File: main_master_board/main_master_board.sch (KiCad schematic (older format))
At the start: 21 parts, among them P1 Hebi_1, P13 CONN_02X20, P2 Hebi_2, P3 Vbackup, P4 CONN_02X05, P5 Mounting Holes, P6 Mounting Holes, P7 Mounting Holes, P8 Mounting Holes, Q3 PSMN013-80YS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

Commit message: Changed expansion connector to two connectors. Routed 5 to 4 buck.
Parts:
- removed P13: CONN_02X20, Hirose:DF40HC(3.0)-40DS-0.4V(51), symbol CONN_02X20
- added P13, P15: CONN_02X15, Hirose:DF40HC(3.5)-30DS-0.4V(51), symbol CONN_02X15
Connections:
- net labels added: GPIO_105, GPIO_106, GPIO_108, GPIO_113, GPIO_114, GPIO_116, GPIO_26, GPIO_27, GPIO_28, GPIO_30, GPIO_49, GPIO_50, GPIO_51, GPIO_52, GPIO_69
- net labels removed: RD9, RF2
- wire segments 215 -> 256
- no-connect marks 1 -> 0
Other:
- moved on the sheet: P5, P6, P7, P8

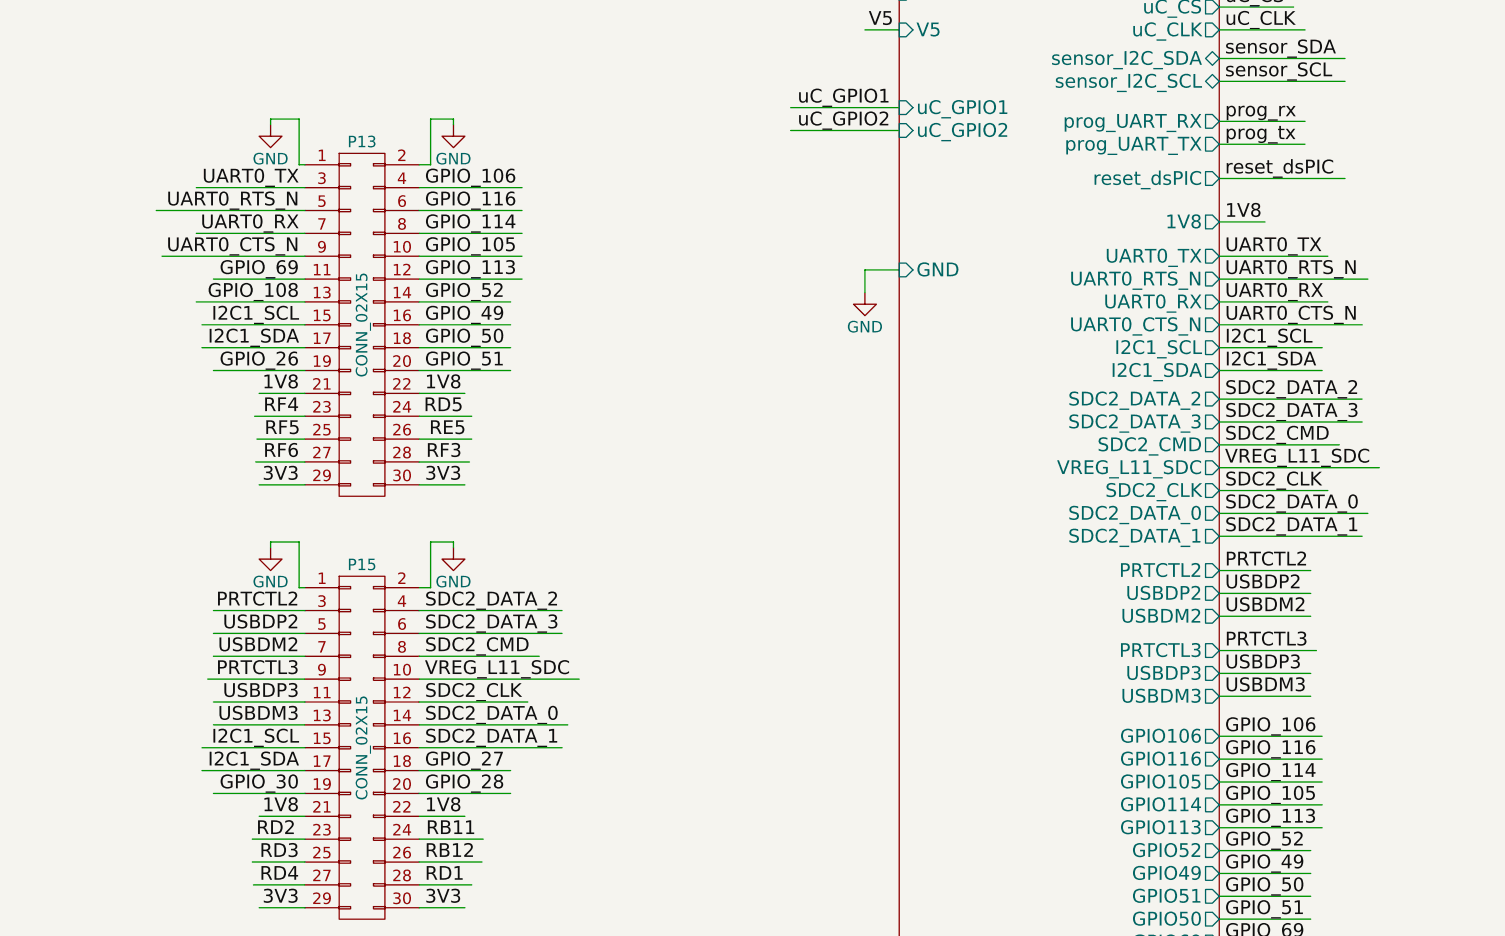
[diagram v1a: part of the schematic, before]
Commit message: Added antenna for DART board. Also fixed 90 pin connector placement (was 180 degrees wrong). Placed Dart Board in position.
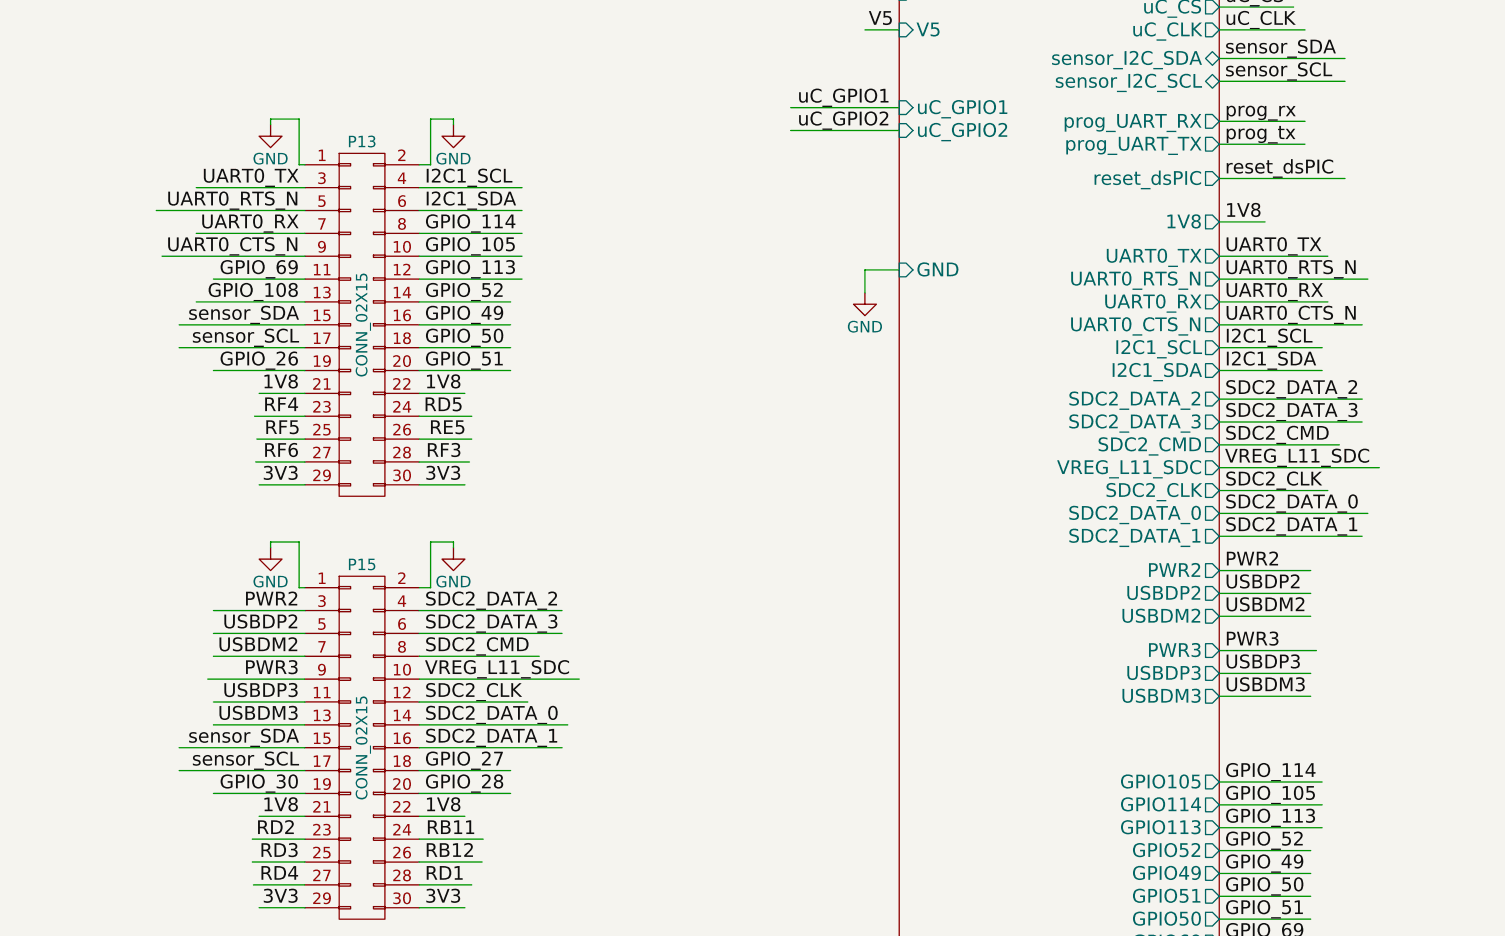
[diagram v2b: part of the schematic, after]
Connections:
- net labels added: PWR2, PWR3
- net labels removed: GPIO_106, GPIO_116, PRTCTL2, PRTCTL3
- wire segments 256 -> 254

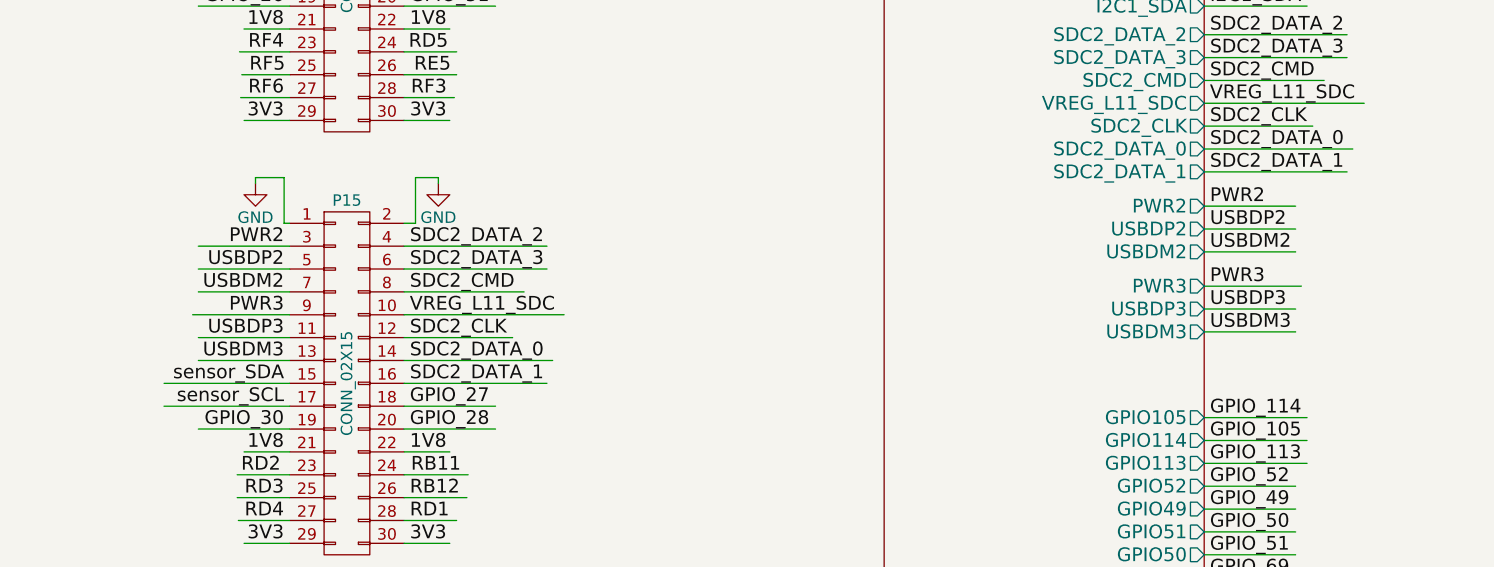
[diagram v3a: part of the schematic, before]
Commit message: Started differential routing for USB and Ethernet.
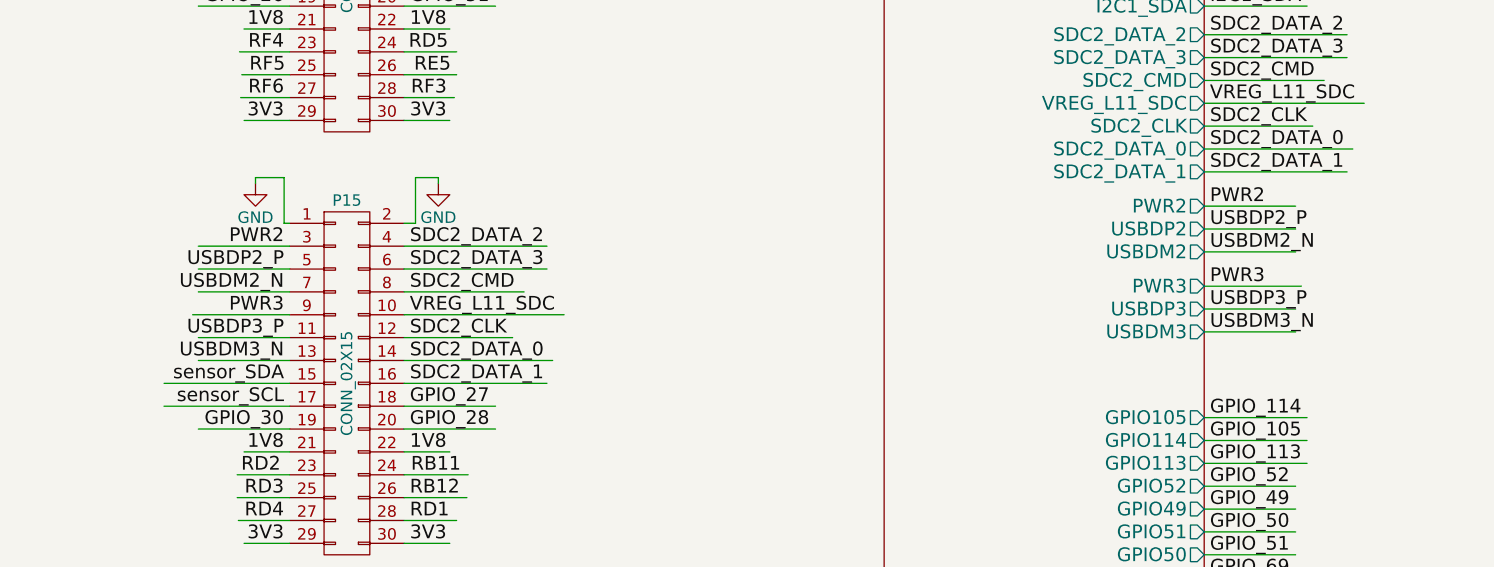
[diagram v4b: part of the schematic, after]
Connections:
- net labels added: USBDM2_N, USBDM3_N, USBDP2_P, USBDP3_P
- net labels removed: USBDM2, USBDM3, USBDP2, USBDP3
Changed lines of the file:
@@
 3V3
 $Comp
-L GNDPWR #PWR8
+L GNDPWR #PWR01
 U 1 1 58756896
 P 2760 2450
-F 0 "#PWR8" H 2760 2250 50  0001 C CNN
+F 0 "#PWR01" H 2760 2250 50  0001 C CNN
 F 1 "GNDPWR" H 2760 2320 50  0000 C CNN
 F 2 "" H 2760 2400 50  0000 C CNN
@@
 $EndComp
 $Comp
-L GND #PWR11
+L GND #PWR02
 U 1 1 58756928
 P 4330 2440
-F 0 "#PWR11" H 4330 2190 50  0001 C CNN
+F 0 "#PWR02" H 4330 2190 50  0001 C CNN
 F 1 "GND" H 4330 2290 50  0000 C CNN
 F 2 "" H 4330 2440 50  0000 C CNN
@@
 Vmotors
 $Comp
-L GND #PWR17
+L GND #PWR03
 U 1 1 5875B134
 P 5225 1790
-F 0 "#PWR17" H 5225 1540 50  0001 C CNN
+F 0 "#PWR03" H 5225 1540 50  0001 C CNN
 F 1 "GND" H 5225 1640 50  0000 C CNN
 F 2 "" H 5225 1790 50  0000 C CNN
@@
 $EndComp
 $Comp
-L GNDPWR #PWR16
+L GNDPWR #PWR04
 U 1 1 5875E5EF
 P 4975 1810
-F 0 "#PWR16" H 4975 1610 50  0001 C CNN
+F 0 "#PWR04" H 4975 1610 50  0001 C CNN
 F 1 "GNDPWR" H 4975 1680 50  0000 C CNN
 F 2 "" H 4975 1760 50  0000 C CNN
@@
 $EndSheet
 $Comp
-L GND #PWR24
+L GND #PWR05
 U 1 1 587B1461
 P 15990 965
-F 0 "#PWR24" H 15990 715 50  0001 C CNN
+F 0 "#PWR05" H 15990 715 50  0001 C CNN
 F 1 "GND" H 15990 815 50  0000 C CNN
 F 2 "" H 15990 965 50  0000 C CNN
@@
 prog_tx
 $Comp
-L GND #PWR23
+L GND #PWR06
 U 1 1 588455B7
 P 13230 6340
-F 0 "#PWR23" H 13230 6090 50  0001 C CNN
+F 0 "#PWR06" H 13230 6090 50  0001 C CNN
 F 1 "GND" H 13230 6190 50  0000 C CNN
 F 2 "" H 13230 6340 50  0000 C CNN
@@
 sensor_SCL
 $Comp
-L GND #PWR22
+L GND #PWR07
 U 1 1 5889E95F
 P 9450 4460
-F 0 "#PWR22" H 9450 4210 50  0001 C CNN
+F 0 "#PWR07" H 9450 4210 50  0001 C CNN
 F 1 "GND" H 9450 4310 50  0000 C CNN
 F 2 "" H 9450 4460 50  0000 C CNN
@@
 Vbackup_in
 $Comp
-L GND #PWR9
+L GND #PWR08
 U 1 1 588D5080
 P 2780 3385
-F 0 "#PWR9" H 2780 3135 50  0001 C CNN
+F 0 "#PWR08" H 2780 3135 50  0001 C CNN
 F 1 "GND" H 2780 3235 50  0000 C CNN
 F 2 "" H 2780 3385 50  0000 C CNN
@@
 V_hebi1
 $Comp
-L GNDPWR #PWR15
+L GNDPWR #PWR09
 U 1 1 588D5095
 P 4785 3330
-F 0 "#PWR15" H 4785 3130 50  0001 C CNN
+F 0 "#PWR09" H 4785 3130 50  0001 C CNN
 F 1 "GNDPWR" H 4785 3200 50  0000 C CNN
 F 2 "" H 4785 3280 50  0000 C CNN
@@
 $EndComp
 $Comp
-L GNDPWR #PWR14
+L GNDPWR #PWR010
 U 1 1 588D509B
 P 4775 3770
-F 0 "#PWR14" H 4775 3570 50  0001 C CNN
+F 0 "#PWR010" H 4775 3570 50  0001 C CNN
 F 1 "GNDPWR" H 4775 3640 50  0000 C CNN
 F 2 "" H 4775 3720 50  0000 C CNN
@@
 $EndComp
 $Comp
-L GNDPWR #PWR1
+L GNDPWR #PWR011
 U 1 1 588D5126
 P 890 3495
-F 0 "#PWR1" H 890 3295 50  0001 C CNN
+F 0 "#PWR011" H 890 3295 50  0001 C CNN
 F 1 "GNDPWR" H 890 3365 50  0000 C CNN
 F 2 "" H 890 3445 50  0000 C CNN
@@
 $EndComp
 $Comp
-L GNDPWR #PWR5
+L GNDPWR #PWR012
 U 1 1 588D512C
 P 1730 4095
-F 0 "#PWR5" H 1730 3895 50  0001 C CNN
+F 0 "#PWR012" H 1730 3895 50  0001 C CNN
 F 1 "GNDPWR" H 1730 3965 50  0000 C CNN
 F 2 "" H 1730 4045 50  0000 C CNN
@@
 ks_nFault_signal
 $Comp
-L GNDPWR #PWR4
+L GNDPWR #PWR013
 U 1 1 588EACE1
 P 1320 2845
-F 0 "#PWR4" H 1320 2645 50  0001 C CNN
+F 0 "#PWR013" H 1320 2645 50  0001 C CNN
 F 1 "GNDPWR" H 1320 2715 50  0000 C CNN
 F 2 "" H 1320 2795 50  0000 C CNN
@@
 V4
 $Comp
-L +24V #PWR7
+L +24V #PWR014
 U 1 1 58919C55
 P 2600 800
-F 0 "#PWR7" H 2600 650 50  0001 C CNN
+F 0 "#PWR014" H 2600 650 50  0001 C CNN
 F 1 "+24V" H 2600 940 50  0000 C CNN
 F 2 "" H 2600 800 50  0000 C CNN
@@
 Switch_on
 $Comp
-L +5V #PWR12
+L +5V #PWR015
 U 1 1 58924C9E
 P 4375 1075
-F 0 "#PWR12" H 4375 925 50  0001 C CNN
+F 0 "#PWR015" H 4375 925 50  0001 C CNN
 F 1 "+5V" H 4375 1215 50  0000 C CNN
 F 2 "" H 4375 1075 50  0000 C CNN
@@
 $EndComp
 $Comp
-L +3V3 #PWR13
+L +3V3 #PWR016
 U 1 1 58925954
 P 4375 1325
-F 0 "#PWR13" H 4375 1175 50  0001 C CNN
+F 0 "#PWR016" H 4375 1175 50  0001 C CNN
 F 1 "+3V3" H 4375 1465 50  0000 C CNN
 F 2 "" H 4375 1325 50  0000 C CNN
@@
 1V8
 $Comp
-L GND #PWR19
+L GND #PWR017
 U 1 1 588DE363
 P 6850 5575
-F 0 "#PWR19" H 6850 5325 50  0001 C CNN
+F 0 "#PWR017" H 6850 5325 50  0001 C CNN
 F 1 "GND" H 6850 5425 50  0000 C CNN
 F 2 "" H 6850 5575 50  0000 C CNN
@@
 1V8
 $Comp
-L GND #PWR21
+L GND #PWR018
 U 1 1 588E75F1
 P 7650 5575
-F 0 "#PWR21" H 7650 5325 50  0001 C CNN
+F 0 "#PWR018" H 7650 5325 50  0001 C CNN
 F 1 "GND" H 7650 5425 50  0000 C CNN
 F 2 "" H 7650 5575 50  0000 C CNN
@@
 VREG_L11_SDC
 Text Label 11025 5775 0    60   ~ 0
-USBDP2
+USBDP2_P
 Text Label 11025 5875 0    60   ~ 0
-USBDM2
+USBDM2_N
 Text Label 11025 6125 0    60   ~ 0
-USBDP3
+USBDP3_P
 Text Label 11025 6225 0    60   ~ 0
-USBDM3
+USBDM3_N
 Text Label 11025 4700 0    60   ~ 0
 I2C1_SCL
@@
 VREG_L11_SDC
 Text Label 6975 6050 2    60   ~ 0
-USBDM2
+USBDM2_N
 Text Label 6975 6250 2    60   ~ 0
-USBDP3
+USBDP3_P
 Text Label 6975 6350 2    60   ~ 0
-USBDM3
+USBDM3_N
 Text Label 6975 4000 2    60   ~ 0
 UART0_TX
@@
 $EndComp
 $Comp
-L GND #PWR6
+L GND #PWR019
 U 1 1 5892EC4B
 P 2450 5475
-F 0 "#PWR6" H 2450 5225 50  0001 C CNN
+F 0 "#PWR019" H 2450 5225 50  0001 C CNN
 F 1 "GND" H 2450 5325 50  0000 C CNN
 F 2 "" H 2450 5475 50  0000 C CNN
@@
 $EndComp
 $Comp
-L GND #PWR3
+L GND #PWR020
 U 1 1 5894DC56
 P 1025 5200
-F 0 "#PWR3" H 1025 4950 50  0001 C CNN
+F 0 "#PWR020" H 1025 4950 50  0001 C CNN
 F 1 "GND" H 1025 5050 50  0000 C CNN
 F 2 "" H 1025 5200 50  0000 C CNN
@@
 	1125 4800 575  4800
 $Comp
-L GND #PWR2
+L GND #PWR021
 U 1 1 589559E0
 P 975 4500
-F 0 "#PWR2" H 975 4250 50  0001 C CNN
+F 0 "#PWR021" H 975 4250 50  0001 C CNN
 F 1 "GND" H 975 4350 50  0000 C CNN
 F 2 "" H 975 4500 50  0000 C CNN
@@
 	15105 6450 15625 6450
 $Comp
-L GND #PWR10
+L GND #PWR022
 U 1 1 589CCB37
 P 3050 5200
-F 0 "#PWR10" H 3050 4950 50  0001 C CNN
+F 0 "#PWR022" H 3050 4950 50  0001 C CNN
 F 1 "GND" H 3050 5050 50  0000 C CNN
 F 2 "" H 3050 5200 50  0000 C CNN
@@
 	7500 6750 7700 6750
 $Comp
-L GND #PWR20
+L GND #PWR023
 U 1 1 58980A8F
 P 7650 3725
-F 0 "#PWR20" H 7650 3475 50  0001 C CNN
+F 0 "#PWR023" H 7650 3475 50  0001 C CNN
 F 1 "GND" H 7650 3575 50  0000 C CNN
 F 2 "" H 7650 3725 50  0000 C CNN
@@
 	7650 3700 7650 3725
 $Comp
-L GND #PWR18
+L GND #PWR024
 U 1 1 5898915B
 P 6850 3725
-F 0 "#PWR18" H 6850 3475 50  0001 C CNN
+F 0 "#PWR024" H 6850 3475 50  0001 C CNN
 F 1 "GND" H 6850 3575 50  0000 C CNN
 F 2 "" H 6850 3725 50  0000 C CNN
@@
 PWR2
 Text Label 6975 5950 2    60   ~ 0
-USBDP2
+USBDP2_P
 Text Label 6975 6150 2    60   ~ 0
 PWR3

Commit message: Started routing usb
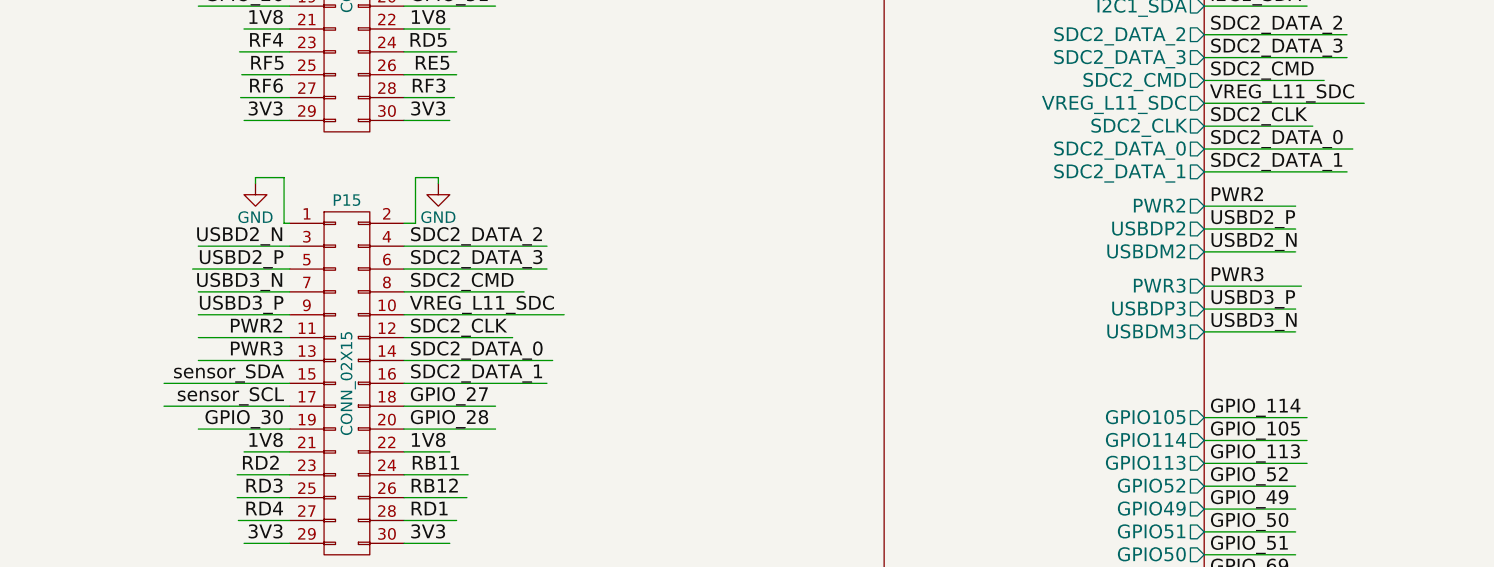
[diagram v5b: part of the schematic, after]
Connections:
- net labels added: USBD2_N, USBD2_P, USBD3_N, USBD3_P
- net labels removed: USBDM2_N, USBDM3_N, USBDP2_P, USBDP3_P
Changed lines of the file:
@@
 Text Label 11025 5225 0    60   ~ 0
 VREG_L11_SDC
-Text Label 11025 5775 0    60   ~ 0
-USBDP2_P
-Text Label 11025 5875 0    60   ~ 0
-USBDM2_N
-Text Label 11025 6125 0    60   ~ 0
-USBDP3_P
-Text Label 11025 6225 0    60   ~ 0
-USBDM3_N
 Text Label 11025 4700 0    60   ~ 0
 I2C1_SCL
@@
 Text Label 7525 6150 0    60   ~ 0
 VREG_L11_SDC
-Text Label 6975 6050 2    60   ~ 0
-USBDM2_N
-Text Label 6975 6250 2    60   ~ 0
-USBDP3_P
-Text Label 6975 6350 2    60   ~ 0
-USBDM3_N
 Text Label 6975 4000 2    60   ~ 0
 UART0_TX
@@
 	7500 6450 8125 6450
 Wire Wire Line
-	7000 5950 6600 5950
+	7000 6350 6600 6350
+Wire Wire Line
+	7000 5850 6600 5850
+Wire Wire Line
+	7000 5950 6575 5950
 Wire Wire Line
 	7000 6050 6600 6050
 Wire Wire Line
-	7000 6150 6575 6150
+	7000 6150 6600 6150
 Wire Wire Line
 	7000 6250 6600 6250
-Wire Wire Line
-	7000 6350 6600 6350
-Wire Wire Line
-	7000 5850 6600 5850
 Wire Wire Line
 	15105 5625 15335 5625
@@
 Text Label 11025 6025 0    60   ~ 0
 PWR3
-Text Label 6975 5850 2    60   ~ 0
+Text Label 6975 6250 2    60   ~ 0
 PWR2
-Text Label 6975 5950 2    60   ~ 0
-USBDP2_P
-Text Label 6975 6150 2    60   ~ 0
+Text Label 6975 6350 2    60   ~ 0
 PWR3
 Text Label 6975 4600 2    60   ~ 0
@@
 Wire Wire Line
 	7500 4100 7950 4100
+Text Label 11025 5775 0    60   ~ 0
+USBD2_P
+Text Label 11025 5875 0    60   ~ 0
+USBD2_N
+Text Label 11025 6125 0    60   ~ 0
+USBD3_P
+Text Label 11025 6225 0    60   ~ 0
+USBD3_N
+Text Label 6975 5950 2    60   ~ 0
+USBD2_P
+Text Label 6975 5850 2    60   ~ 0
+USBD2_N
+Text Label 6975 6150 2    60   ~ 0
+USBD3_P
+Text Label 6975 6050 2    60   ~ 0
+USBD3_N
 $EndSCHEMATC
